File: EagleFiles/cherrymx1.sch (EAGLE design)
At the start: 22 parts, among them Q1 MMBT2222A, Y1 16MHz

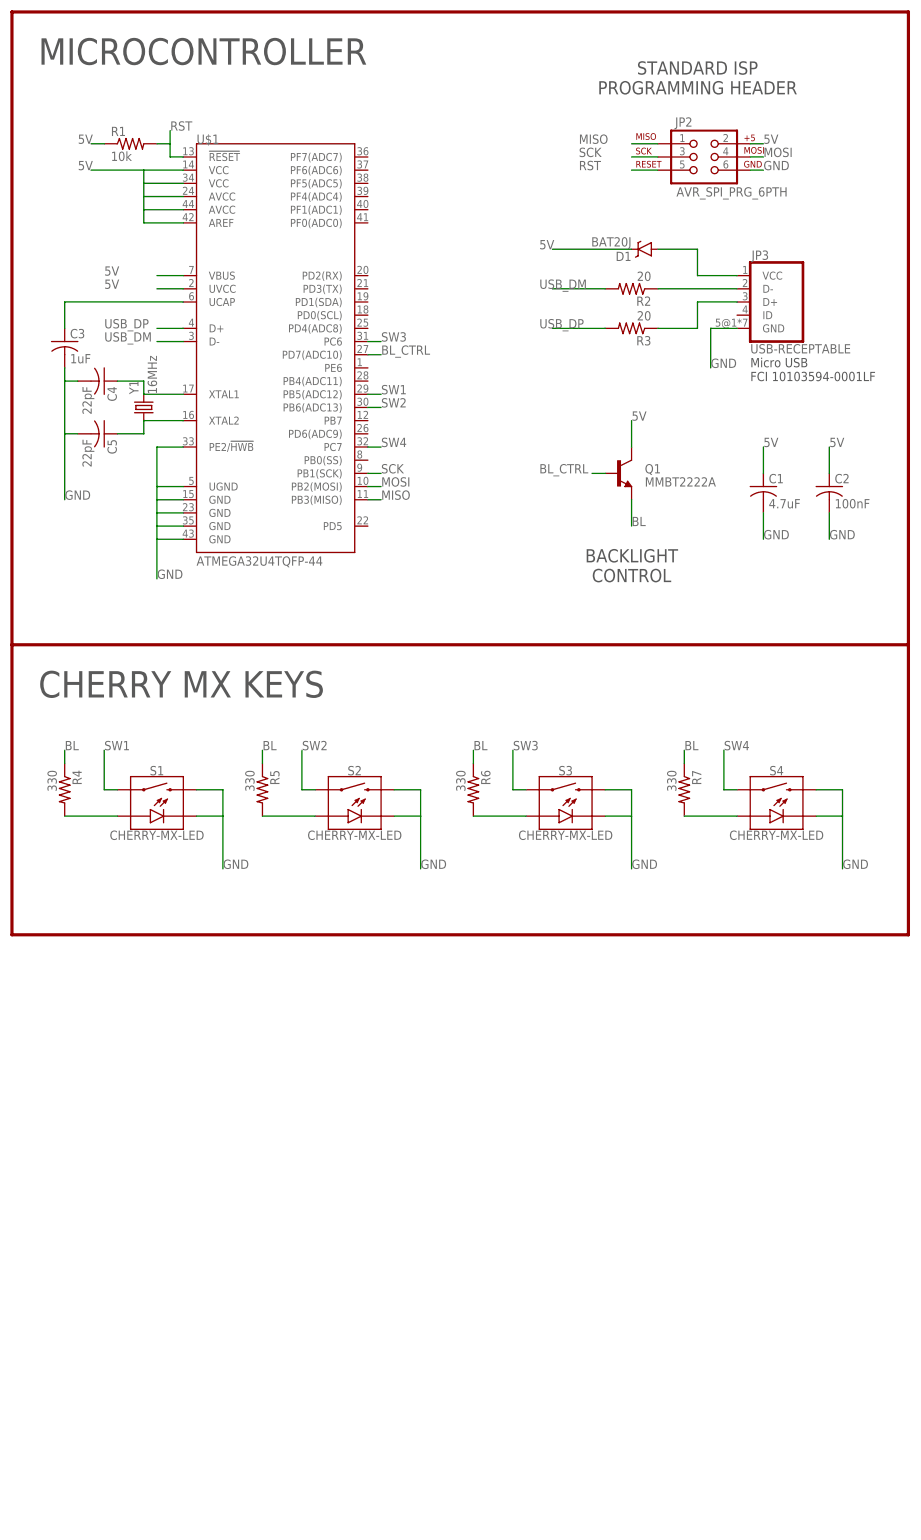
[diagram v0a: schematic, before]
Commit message: Add a bunch more switches!
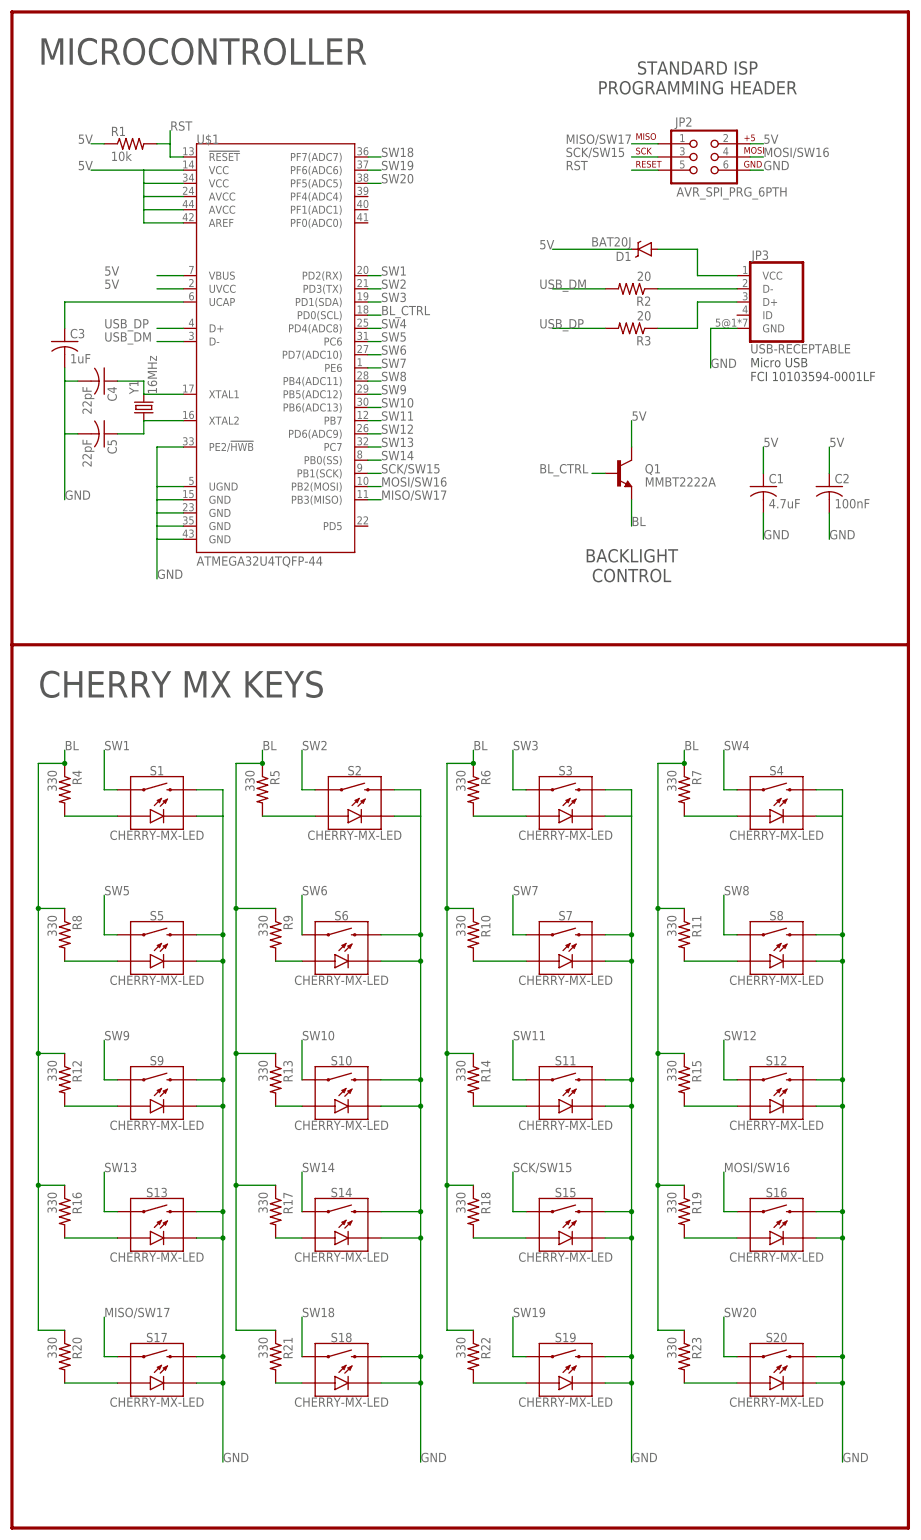
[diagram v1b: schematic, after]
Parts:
- added R10, R11, R12, R13, R14, R15, R16, R17, R18, R19, R20, R21, R22, R23, R8, R9: 330, adafruit:R-US_R0603
- added S10, S11, S12, S13, S14, S15, S16, S17, S18, S19, S20, S5, S6, S7, S8, S9: CHERRY-MX-LED, SparkFun-Electromechanical2:CHERRY-MX-LED
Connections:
- removed net MISO: JP2.1, U$1.PB3(MISO)
- removed net MOSI: JP2.4, U$1.PB2(MOSI)
- removed net SCK: JP2.3, U$1.PB1(SCK)
- new net MISO/SW17: JP2.1, S17.S1, U$1.PB3(MISO)
- new net MOSI/SW16: JP2.4, S16.S1, U$1.PB2(MOSI)
- new net N$13: R16.2, S13.A
- new net N$14: R20.2, S17.A
- new net N$15: R21.2, S18.A
- new net N$16: R17.2, S14.A
- new net N$17: R13.2, S10.A
- new net N$18: R9.2, S6.A
- new net N$19: R22.2, S19.A
- new net N$20: R18.2, S15.A
- new net N$21: R14.2, S11.A
- new net N$22: R10.2, S7.A
- new net N$23: R23.2, S20.A
- new net N$24: R19.2, S16.A
- new net N$25: R15.2, S12.A
- new net N$26: R11.2, S8.A
- new net N$4: R8.2, S5.A
- new net N$7: R12.2, S9.A
- new net SCK/SW15: JP2.3, S15.S1, U$1.PB1(SCK)
- new net SW10: S10.S1, U$1.PB6(ADC13)
- new net SW11: S11.S1, U$1.PB7
- new net SW12: S12.S1, U$1.PD6(ADC9)
- new net SW13: S13.S1, U$1.PC7
- new net SW14: S14.S1, U$1.PB0(SS)
- new net SW18: S18.S1, U$1.PF7(ADC7)
- new net SW19: S19.S1, U$1.PF6(ADC6)
- new net SW20: S20.S1, U$1.PF5(ADC5)
- new net SW5: S5.S1, U$1.PC6
- new net SW6: S6.S1, U$1.PD7(ADC10)
- new net SW7: S7.S1, U$1.PE6
- new net SW8: S8.S1, U$1.PB4(ADC11)
- new net SW9: S9.S1, U$1.PB5(ADC12)
- net BL: now also R10.1, R11.1, R12.1, R13.1, R14.1, R15.1, R16.1, R17.1, R18.1, R19.1, R20.1, R21.1, R22.1, R23.1, R8.1, R9.1
- net BL_CTRL: now also U$1.PD0(SCL); no longer U$1.PD7(ADC10)
- net GND: now also S10.C, S10.S2, S11.C, S11.S2, S12.C, S12.S2, S13.C, S13.S2, S14.C, S14.S2, S15.C, S15.S2, S16.C, S16.S2, S17.C, S17.S2, S18.C, S18.S2, S19.C, S19.S2, S20.C, S20.S2, S5.C, S5.S2, S6.C, S6.S2, S7.C, S7.S2, S8.C, S8.S2, S9.C, S9.S2
- net SW1: now also U$1.PD2(RX); no longer U$1.PB5(ADC12)
- net SW2: now also U$1.PD3(TX); no longer U$1.PB6(ADC13)
- net SW3: now also U$1.PD1(SDA); no longer U$1.PC6
- net SW4: now also U$1.PD4(ADC8); no longer U$1.PC7
